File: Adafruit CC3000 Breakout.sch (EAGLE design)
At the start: 34 parts, among them IC1 ATmega1284P, U1 CC3000MOD, X1 2500AT44M0400E

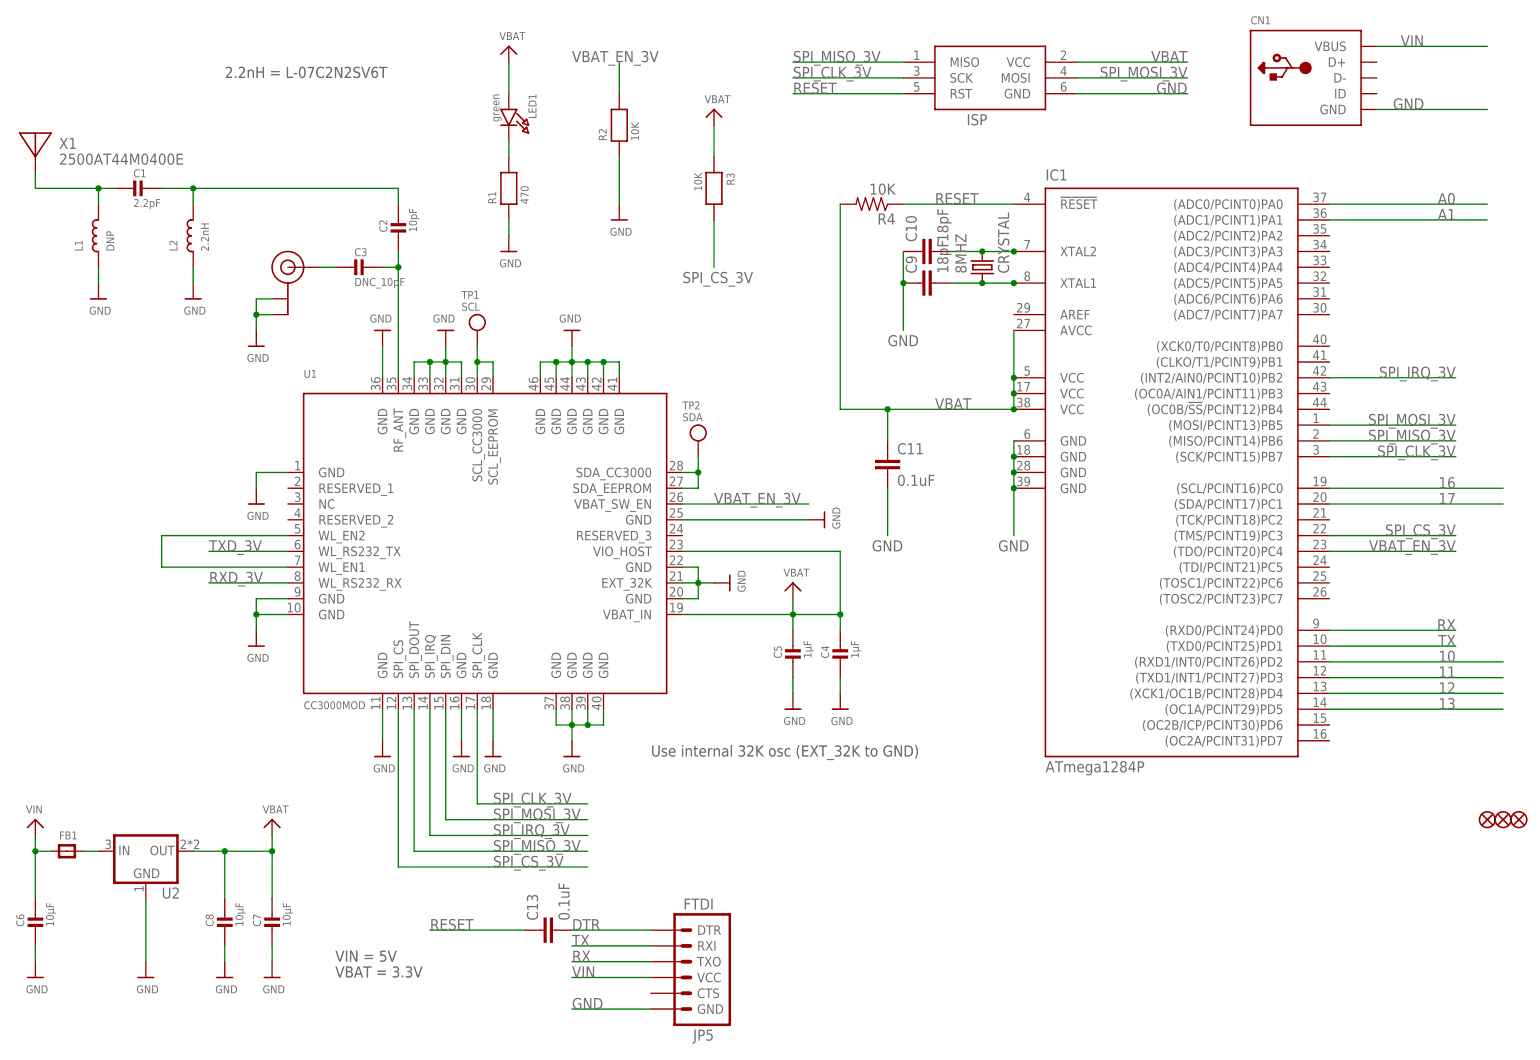
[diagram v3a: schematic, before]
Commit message: Replace passives (w/ 1206), re-layout components.
Also, change pinouts on the ATmega1284P to match the Wicked Devices
Wildfire prototyping board. Remove rounded corners.
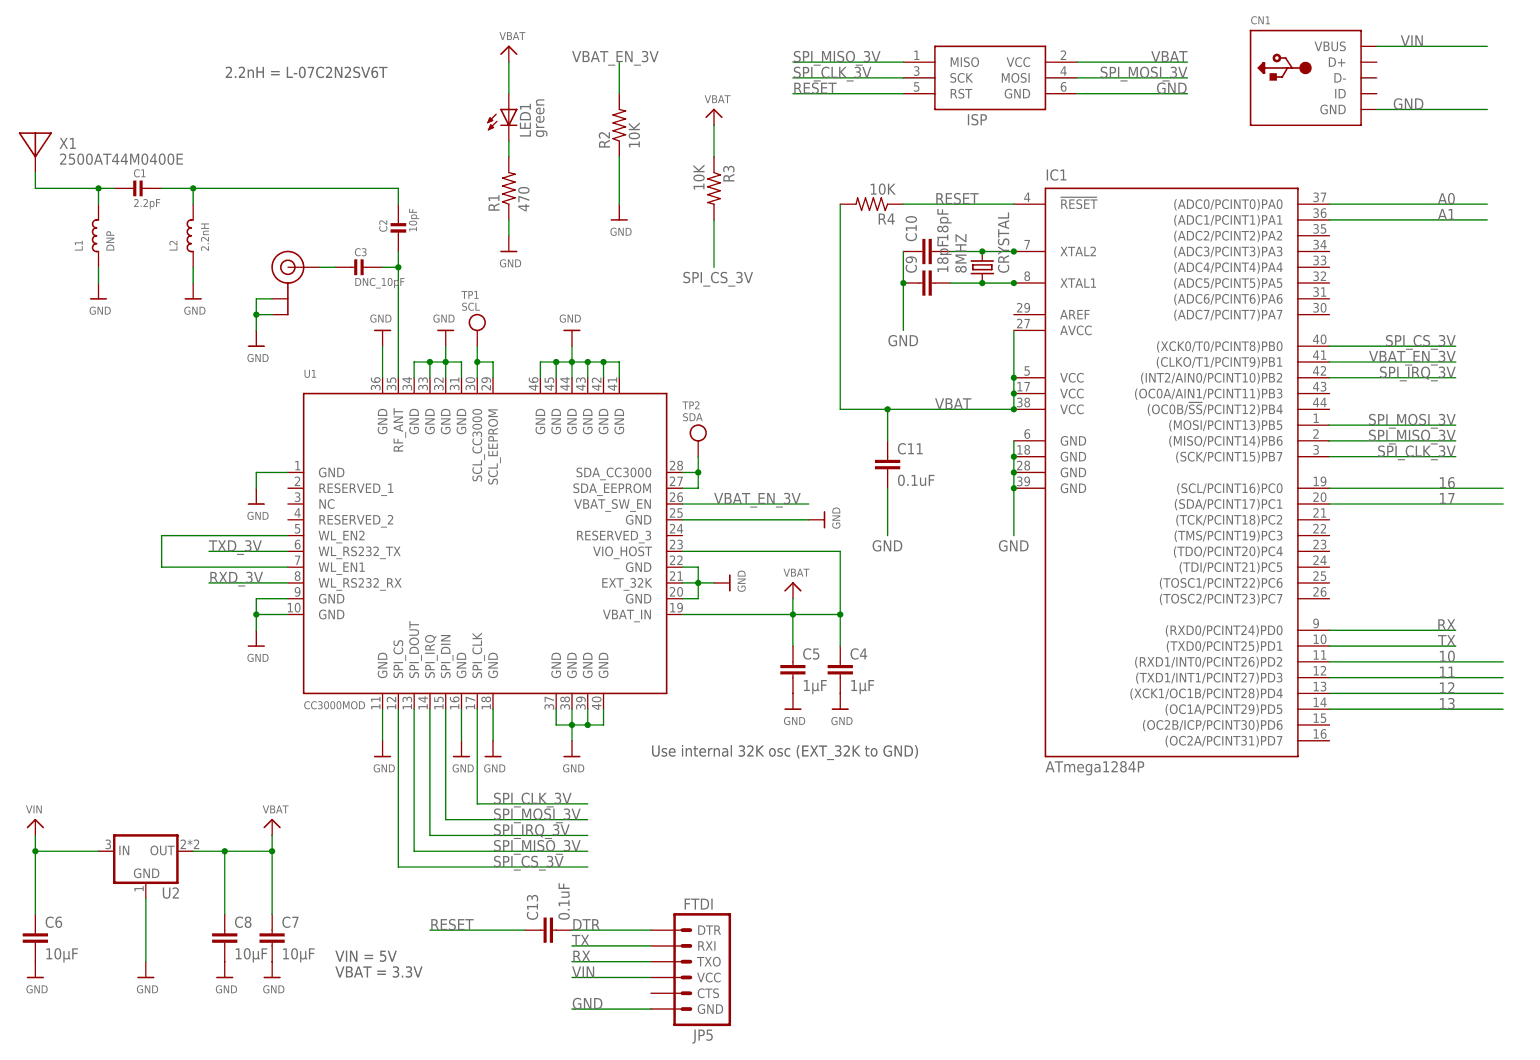
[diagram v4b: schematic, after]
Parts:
- removed FB1: (no value), microbuilder:FERRITE_0805MP
- removed FID1, FID2, FID3: FIDUCIAL"", microbuilder:FIDUCIAL""
- C4, C5, C6, C7, C8: device microbuilder:CAP_CERAMIC_0805MP -> rcl:C-EUC1206
- LED1: device microbuilder:LED0805_NOOUTLINE -> led:LEDSMT1206
- R1: device microbuilder:RESISTOR0805_NOOUTLINE -> rcl:R-US_R1206
- R2, R3: device microbuilder:RESISTOR_0805MP -> rcl:R-US_R1206
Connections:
- removed net N$9: FB1.P$2, U2.IN
- net SPI_CS_3V: now also IC1.(XCK0/T0/PCINT8)PB0; no longer IC1.(TMS/PCINT19)PC3
- net VBAT_EN_3V: now also IC1.(CLKO/T1/PCINT9)PB1; no longer IC1.(TDO/PCINT20)PC4
- net VIN: now also U2.IN; no longer FB1.P$1
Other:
- moved on the sheet: C4, C5, C6, C7, C8
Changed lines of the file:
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@@
 <part name="U$7" library="microbuilder" deviceset="GND" device=""/>
 <part name="U$9" library="microbuilder" deviceset="GND" device=""/>
-<part name="C4" library="microbuilder" deviceset="CAP_CERAMIC" device="_0805MP" value="1µF"/>
-<part name="C5" library="microbuilder" deviceset="CAP_CERAMIC" device="_0805MP" value="1µF"/>
+<part name="C4" library="rcl" deviceset="C-EU" device="C1206" value="1µF"/>
+<part name="C5" library="rcl" deviceset="C-EU" device="C1206" value="1µF"/>
 <part name="U$10" library="microbuilder" deviceset="GND" device=""/>
 <part name="U$11" library="microbuilder" deviceset="VBAT" device=""/>
@@
 <part name="U$19" library="microbuilder" deviceset="GND" device=""/>
 <part name="U$20" library="microbuilder" deviceset="GND" device=""/>
-<part name="FID1" library="microbuilder" deviceset="FIDUCIAL" device="&quot;&quot;"/>
-<part name="FID2" library="microbuilder" deviceset="FIDUCIAL" device="&quot;&quot;"/>
-<part name="C6" library="microbuilder" deviceset="CAP_CERAMIC" device="_0805MP" value="10µF"/>
-<part name="C7" library="microbuilder" deviceset="CAP_CERAMIC" device="_0805MP" value="10µF"/>
+<part name="C6" library="rcl" deviceset="C-EU" device="C1206" value="10µF"/>
+<part name="C7" library="rcl" deviceset="C-EU" device="C1206" value="10µF"/>
 <part name="U$25" library="microbuilder" deviceset="VIN" device=""/>
 <part name="U$26" library="microbuilder" deviceset="VBAT" device=""/>
@@
 <part name="U$28" library="microbuilder" deviceset="GND" device=""/>
 <part name="U2" library="microbuilder" deviceset="VREG_SOT223" device=""/>
-<part name="C8" library="microbuilder" deviceset="CAP_CERAMIC" device="_0805MP" value="10µF"/>
+<part name="C8" library="rcl" deviceset="C-EU" device="C1206" value="10µF"/>
 <part name="U$29" library="microbuilder" deviceset="GND" device=""/>
 <part name="U$30" library="microbuilder" deviceset="GND" device=""/>
-<part name="FB1" library="microbuilder" deviceset="FERRITE" device="_0805MP"/>
 <part name="TP1" library="microbuilder" deviceset="TESTPOINT" device="PAD1MM" value="SCL"/>
 <part name="TP2" library="microbuilder" deviceset="TESTPOINT" device="PAD1MM" value="SDA"/>
-<part name="R2" library="microbuilder" deviceset="RESISTOR" device="_0805MP" value="10K"/>
+<part name="R2" library="rcl" deviceset="R-US_" device="R1206" value="10K"/>
 <part name="U$14" library="microbuilder" deviceset="GND" device=""/>
-<part name="R3" library="microbuilder" deviceset="RESISTOR" device="_0805MP" value="10K"/>
+<part name="R3" library="rcl" deviceset="R-US_" device="R1206" value="10K"/>
 <part name="U$22" library="microbuilder" deviceset="VBAT" device=""/>
 <part name="U$35" library="microbuilder" deviceset="U.FL" device=""/>
-<part name="FID3" library="microbuilder" deviceset="FIDUCIAL" device="&quot;&quot;">
-<attribute name="BOM" value="EXCLUDE"/>
-</part>
-<part name="LED1" library="microbuilder" deviceset="LED" device="0805_NOOUTLINE" value="green"/>
-<part name="R1" library="microbuilder" deviceset="RESISTOR" device="0805_NOOUTLINE" value="470"/>
+<part name="LED1" library="led" deviceset="LED" device="SMT1206" value="green"/>
+<part name="R1" library="rcl" deviceset="R-US_" device="R1206" value="470"/>
 <part name="U$37" library="microbuilder" deviceset="GND" device=""/>
 <part name="U$38" library="microbuilder" deviceset="VBAT" device=""/>
@@
 <instance part="U$19" gate="G$1" x="50.8" y="68.58"/>
 <instance part="U$20" gate="G$1" x="50.8" y="91.44"/>
-<instance part="FID1" gate="G$1" x="254" y="40.64"/>
-<instance part="FID2" gate="G$1" x="248.92" y="40.64"/>
 <instance part="C6" gate="G$1" x="15.24" y="22.86"/>
 <instance part="C7" gate="G$1" x="53.34" y="22.86"/>
@@
 <instance part="U$29" gate="G$1" x="45.72" y="15.24"/>
 <instance part="U$30" gate="G$1" x="33.02" y="15.24"/>
-<instance part="FB1" gate="G$1" x="20.32" y="35.56"/>
 <instance part="TP1" gate="G$1" x="86.36" y="116.84"/>
 <instance part="TP2" gate="G$1" x="121.92" y="99.06"/>
@@
 <instance part="U$22" gate="G$1" x="124.46" y="154.94"/>
 <instance part="U$35" gate="G$1" x="55.88" y="129.54"/>
-<instance part="FID3" gate="G$1" x="251.46" y="40.64"/>
-<instance part="LED1" gate="G$1" x="91.44" y="152.4" rot="R270"/>
+<instance part="LED1" gate="G$1" x="91.44" y="154.94"/>
 <instance part="R1" gate="G$1" x="91.44" y="142.24" rot="R90"/>
 <instance part="U$37" gate="G$1" x="91.44" y="132.08"/>
@@
 <pinref part="C4" gate="G$1" pin="2"/>
 <pinref part="U$9" gate="G$1" pin="GND"/>
-<wire x1="144.78" y1="63.5" x2="144.78" y2="60.96" width="0.1524" layer="91"/>
 </segment>
 <segment>
 <pinref part="C5" gate="G$1" pin="2"/>
 <pinref part="U$10" gate="G$1" pin="GND"/>
-<wire x1="137.16" y1="63.5" x2="137.16" y2="60.96" width="0.1524" layer="91"/>
 </segment>
 <segment>
@@
 <pinref part="C7" gate="G$1" pin="2"/>
 <pinref part="U$28" gate="G$1" pin="GND"/>
-<wire x1="53.34" y1="20.32" x2="53.34" y2="17.78" width="0.1524" layer="91"/>
 </segment>
 <segment>
 <pinref part="C6" gate="G$1" pin="2"/>
 <pinref part="U$27" gate="G$1" pin="GND"/>
-<wire x1="15.24" y1="20.32" x2="15.24" y2="17.78" width="0.1524" layer="91"/>
 </segment>
 <segment>
 <pinref part="C8" gate="G$1" pin="2"/>
 <pinref part="U$29" gate="G$1" pin="GND"/>
-<wire x1="45.72" y1="20.32" x2="45.72" y2="17.78" width="0.1524" layer="91"/>
 </segment>
 <segment>
@@
 </segment>
 </net>
-<net name="VBAT" class="0">
+<net name="VBAT" class="1">
 <segment>
 <pinref part="U1" gate="G$1" pin="VBAT_IN"/>
 <pinref part="C5" gate="G$1" pin="1"/>
 <wire x1="119.38" y1="73.66" x2="137.16" y2="73.66" width="0.1524" layer="91"/>
-<wire x1="137.16" y1="73.66" x2="137.16" y2="71.12" width="0.1524" layer="91"/>
+<wire x1="137.16" y1="73.66" x2="137.16" y2="68.58" width="0.1524" layer="91"/>
 <pinref part="U$11" gate="G$1" pin="VBAT"/>
 <wire x1="137.16" y1="73.66" x2="137.16" y2="76.2" width="0.1524" layer="91"/>
@@
 <wire x1="144.78" y1="83.82" x2="144.78" y2="73.66" width="0.1524" layer="91"/>
 <pinref part="C4" gate="G$1" pin="1"/>
-<wire x1="144.78" y1="73.66" x2="144.78" y2="71.12" width="0.1524" layer="91"/>
+<wire x1="144.78" y1="73.66" x2="144.78" y2="68.58" width="0.1524" layer="91"/>
 <junction x="144.78" y="73.66"/>
 </segment>
@@
 <wire x1="53.34" y1="35.56" x2="53.34" y2="38.1" width="0.1524" layer="91"/>
 <pinref part="C7" gate="G$1" pin="1"/>
-<wire x1="53.34" y1="35.56" x2="53.34" y2="27.94" width="0.1524" layer="91"/>
+<wire x1="53.34" y1="35.56" x2="53.34" y2="25.4" width="0.1524" layer="91"/>
 <junction x="53.34" y="35.56"/>
 <pinref part="U2" gate="G$1" pin="OUT"/>
 <pinref part="C8" gate="G$1" pin="1"/>
-<wire x1="45.72" y1="27.94" x2="45.72" y2="35.56" width="0.1524" layer="91"/>
+<wire x1="45.72" y1="25.4" x2="45.72" y2="35.56" width="0.1524" layer="91"/>
 <junction x="45.72" y="35.56"/>
 </segment>
@@
 </segment>
 <segment>
-<pinref part="IC1" gate="G$1" pin="(TDO/PCINT20)PC4"/>
-<wire x1="223.52" y1="83.82" x2="243.84" y2="83.82" width="0.1524" layer="91"/>
-<label x="243.84" y="83.82" size="1.778" layer="95" rot="MR0"/>
-</segment>
-<segment>
 <label x="101.6" y="162.56" size="1.778" layer="95"/>
 <pinref part="R2" gate="G$1" pin="2"/>
 <wire x1="109.22" y1="162.56" x2="109.22" y2="157.48" width="0.1524" layer="91"/>
+</segment>
+<segment>
+<pinref part="IC1" gate="G$1" pin="(CLKO/T1/PCINT9)PB1"/>
+<wire x1="223.52" y1="114.3" x2="243.84" y2="114.3" width="0.1524" layer="91"/>
+<label x="243.84" y="114.3" size="1.778" layer="95" rot="MR0"/>
 </segment>
 </net>
@@
 </segment>
 <segment>
-<pinref part="IC1" gate="G$1" pin="(TMS/PCINT19)PC3"/>
-<wire x1="223.52" y1="86.36" x2="243.84" y2="86.36" width="0.1524" layer="91"/>
-<label x="243.84" y="86.36" size="1.778" layer="95" rot="MR0"/>
-</segment>
-<segment>
 <wire x1="124.46" y1="129.54" x2="124.46" y2="137.16" width="0.1524" layer="91"/>
 <label x="119.38" y="127" size="1.778" layer="95"/>
 <pinref part="R3" gate="G$1" pin="2"/>
+</segment>
+<segment>
+<pinref part="IC1" gate="G$1" pin="(XCK0/T0/PCINT8)PB0"/>
+<wire x1="223.52" y1="116.84" x2="243.84" y2="116.84" width="0.1524" layer="91"/>
+<label x="243.84" y="116.84" size="1.778" layer="95" rot="MR0"/>
 </segment>
 </net>
@@
 </segment>
 </net>
-<net name="VIN" class="0">
+<net name="VIN" class="1">
 <segment>
 <pinref part="U$25" gate="G$1" pin="VIN"/>
 <wire x1="15.24" y1="35.56" x2="15.24" y2="38.1" width="0.1524" layer="91"/>
 <pinref part="C6" gate="G$1" pin="1"/>
-<wire x1="15.24" y1="35.56" x2="15.24" y2="27.94" width="0.1524" layer="91"/>
-<pinref part="FB1" gate="G$1" pin="P$1"/>
-<wire x1="17.78" y1="35.56" x2="15.24" y2="35.56" width="0.1524" layer="91"/>
+<wire x1="15.24" y1="35.56" x2="15.24" y2="25.4" width="0.1524" layer="91"/>
 <junction x="15.24" y="35.56"/>
+<pinref part="U2" gate="G$1" pin="IN"/>
+<wire x1="15.24" y1="35.56" x2="25.4" y2="35.56" width="0.1524" layer="91"/>
 </segment>
 <segment>
@@
 </segment>
 </net>
-<net name="N$9" class="0">
-<segment>
-<pinref part="U2" gate="G$1" pin="IN"/>
-<pinref part="FB1" gate="G$1" pin="P$2"/>
-<wire x1="25.4" y1="35.56" x2="22.86" y2="35.56" width="0.1524" layer="91"/>
-</segment>
-</net>
